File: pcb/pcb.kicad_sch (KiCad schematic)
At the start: 5 parts, among them J1 LM2596 OUTPUT, J2 PCA9685, J3 20A 300W High-Power Buck Conv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, J4 ESP32_1, J5 ESP32_2

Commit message: Add 3D models to footprints in PCB for screw terminals and female pin sockets.
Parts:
- J1, J3: footprint TerminalBlock_Altech:Altech_AK100_1x02_P5.00mm -> TerminalBlock:TerminalBlock_MaiXu_MX126-5.0-02P_1x02_P5.00mm
- J2: footprint Connector_PinHeader_2.54mm:PinHeader_1x06_P2.54mm_Vertical -> Connector_PinSocket_2.54mm:PinSocket_1x06_P2.54mm_Horizontal
- J4, J5: footprint Connector_PinHeader_2.54mm:PinHeader_1x19_P2.54mm_Vertical -> Connector_PinSocket_2.54mm:PinSocket_1x19_P2.54mm_Vertical
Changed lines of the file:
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@@
 			)
 		)
-		(property "Footprint" "Connector_PinHeader_2.54mm:PinHeader_1x06_P2.54mm_Vertical"
+		(property "Footprint" "Connector_PinSocket_2.54mm:PinSocket_1x06_P2.54mm_Horizontal"
 			(at 180.34 72.39 0)
 			(effects
@@
 			)
 		)
-		(property "Footprint" "Connector_PinHeader_2.54mm:PinHeader_1x19_P2.54mm_Vertical"
+		(property "Footprint" "Connector_PinSocket_2.54mm:PinSocket_1x19_P2.54mm_Vertical"
 			(at 123.19 82.55 0)
 			(effects
@@
 			)
 		)
-		(property "Footprint" "Connector_PinHeader_2.54mm:PinHeader_1x19_P2.54mm_Vertical"
+		(property "Footprint" "Connector_PinSocket_2.54mm:PinSocket_1x19_P2.54mm_Vertical"
 			(at 135.89 82.55 0)
 			(effects
@@
 			)
 		)
-		(property "Footprint" "TerminalBlock_Altech:Altech_AK100_1x02_P5.00mm"
+		(property "Footprint" "TerminalBlock:TerminalBlock_MaiXu_MX126-5.0-02P_1x02_P5.00mm"
 			(at 180.34 88.9 0)
 			(effects
@@
 			)
 		)
-		(property "Footprint" "TerminalBlock_Altech:Altech_AK100_1x02_P5.00mm"
+		(property "Footprint" "TerminalBlock:TerminalBlock_MaiXu_MX126-5.0-02P_1x02_P5.00mm"
 			(at 180.34 100.33 0)
 			(effects

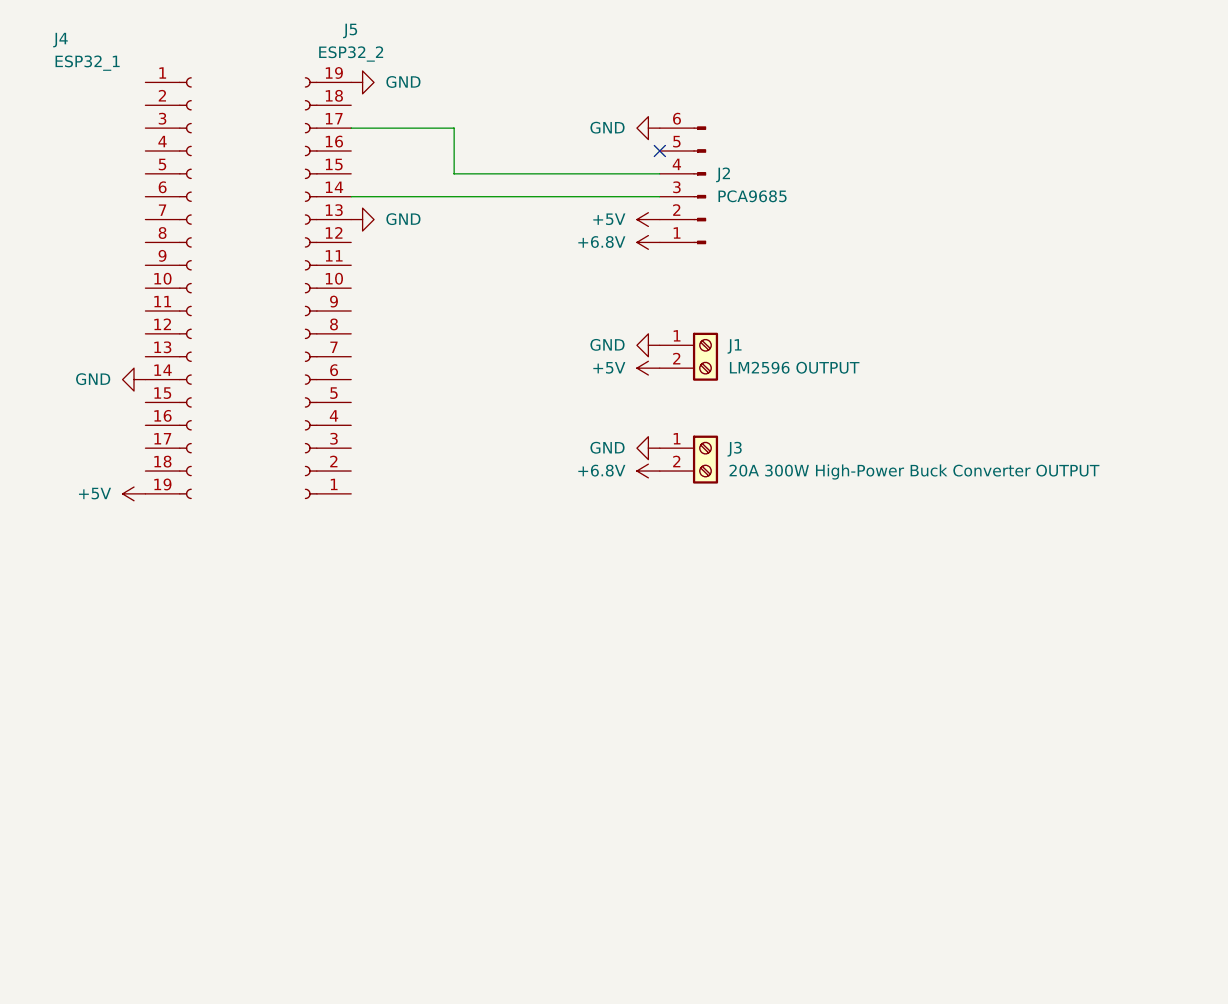
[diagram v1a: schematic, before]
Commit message: Modify power management on PCB. Battery, high power buck converter I/O & low power buck converter input remain off board. Reduce screw hole size.
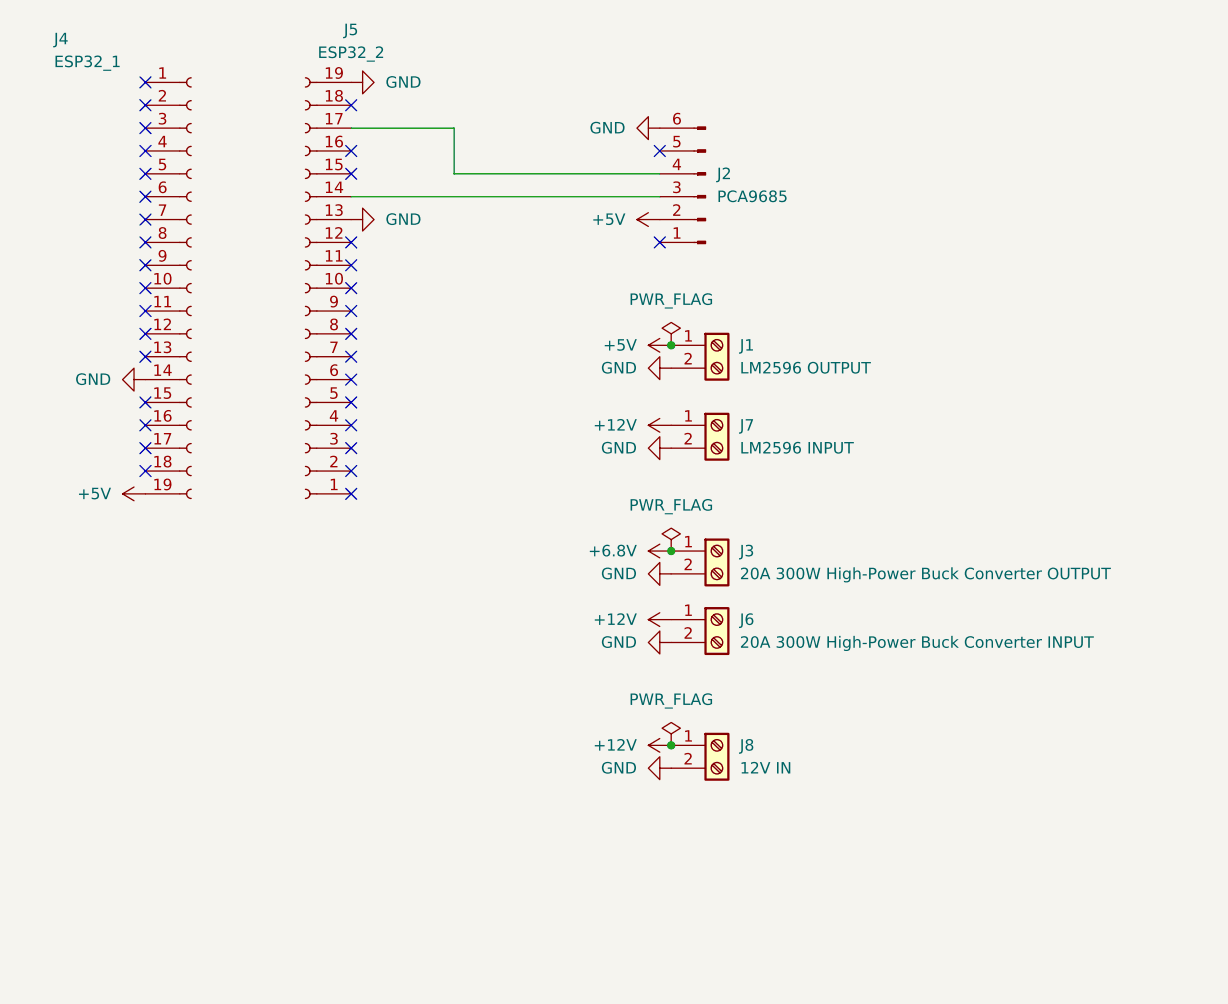
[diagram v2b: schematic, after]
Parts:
- added J6: 20A 300W High-Power Buck Converter INPUT, TerminalBlock:TerminalBlock_MaiXu_MX126-5.0-02P_1x02_P5.00mm, symbol Connector:Screw_Terminal_01x02
- added J7: LM2596 INPUT, TerminalBlock:TerminalBlock_MaiXu_MX126-5.0-02P_1x02_P5.00mm, symbol Connector:Screw_Terminal_01x02
- added J8: 12V IN, TerminalBlock:TerminalBlock_MaiXu_MX126-5.0-02P_1x02_P5.00mm, symbol Connector:Screw_Terminal_01x02
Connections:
- net +5V: now also J1.1 (Pin_1); no longer J1.2 (Pin_2)
- net +6.8V: now also J3.1 (Pin_1); no longer J2.1 (Pin_1), J3.2 (Pin_2)
- net GND: now also J1.2 (Pin_2), J3.2 (Pin_2), J6.2 (Pin_2), J7.2 (Pin_2), J8.2 (Pin_2); no longer J1.1 (Pin_1), J3.1 (Pin_1)
- new net +12V: J6.1 (Pin_1), J7.1 (Pin_1), J8.1 (Pin_1)
- no-connect marks 1 -> 34
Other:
- moved on the sheet: J1, J3

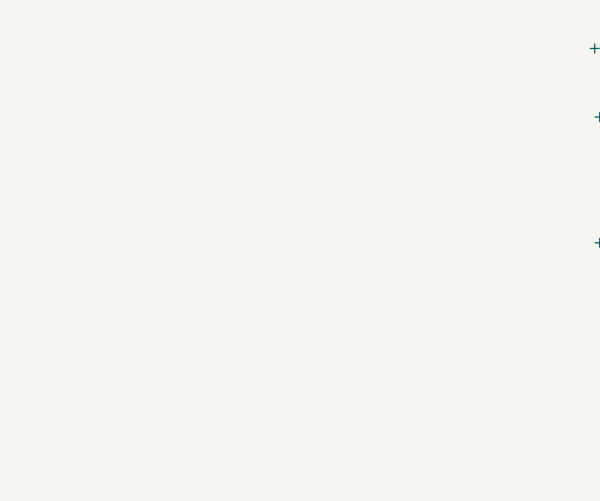
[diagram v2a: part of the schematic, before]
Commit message: Fix: Add dedicated 6.8V copper fill to PCB where a 1x12 header pin is used to power servos. Fixes bottleneck of using the PCA9685 chip to power the servos (doesn't allow for 20A stall current due to simple PCB traces.)
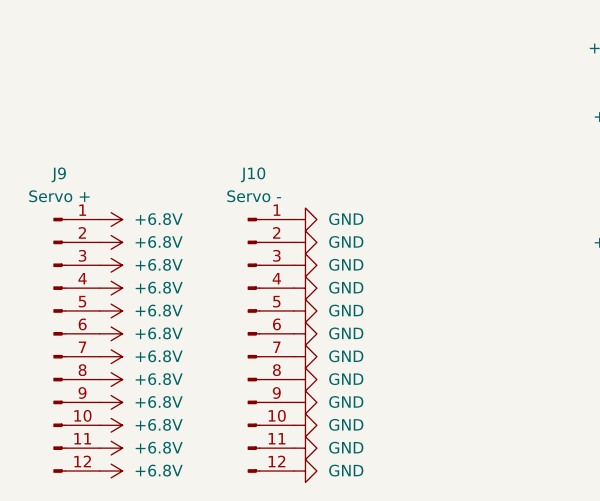
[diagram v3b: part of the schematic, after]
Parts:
- added J10: Servo -, symbol Connector:Conn_01x12_Pin
- added J9: Servo +, Connector_PinHeader_2.54mm:PinHeader_1x12_P2.54mm_Vertical, symbol Connector:Conn_01x12_Pin
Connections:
- net +6.8V: now also J9.1 (Pin_1), J9.10 (Pin_10), J9.11 (Pin_11), J9.12 (Pin_12), J9.2 (Pin_2), J9.3 (Pin_3), J9.4 (Pin_4), J9.5 (Pin_5), J9.6 (Pin_6), J9.7 (Pin_7), J9.8 (Pin_8), J9.9 (Pin_9)
- net GND: now also J10.1 (Pin_1), J10.10 (Pin_10), J10.11 (Pin_11), J10.12 (Pin_12), J10.2 (Pin_2), J10.3 (Pin_3), J10.4 (Pin_4), J10.5 (Pin_5), J10.6 (Pin_6), J10.7 (Pin_7), J10.8 (Pin_8), J10.9 (Pin_9)
